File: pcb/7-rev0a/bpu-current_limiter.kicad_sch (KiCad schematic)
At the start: 44 parts, among them Q401 BCM857, Q402 BC2301T 2.8A, Q601 MMDT3906, Q602 BC2301T 2.8A, U4 MCP4725xxx-xCH, U5 MCP4725xxx-xCH, U601 GS321A-TR, U602 GSV331-TR

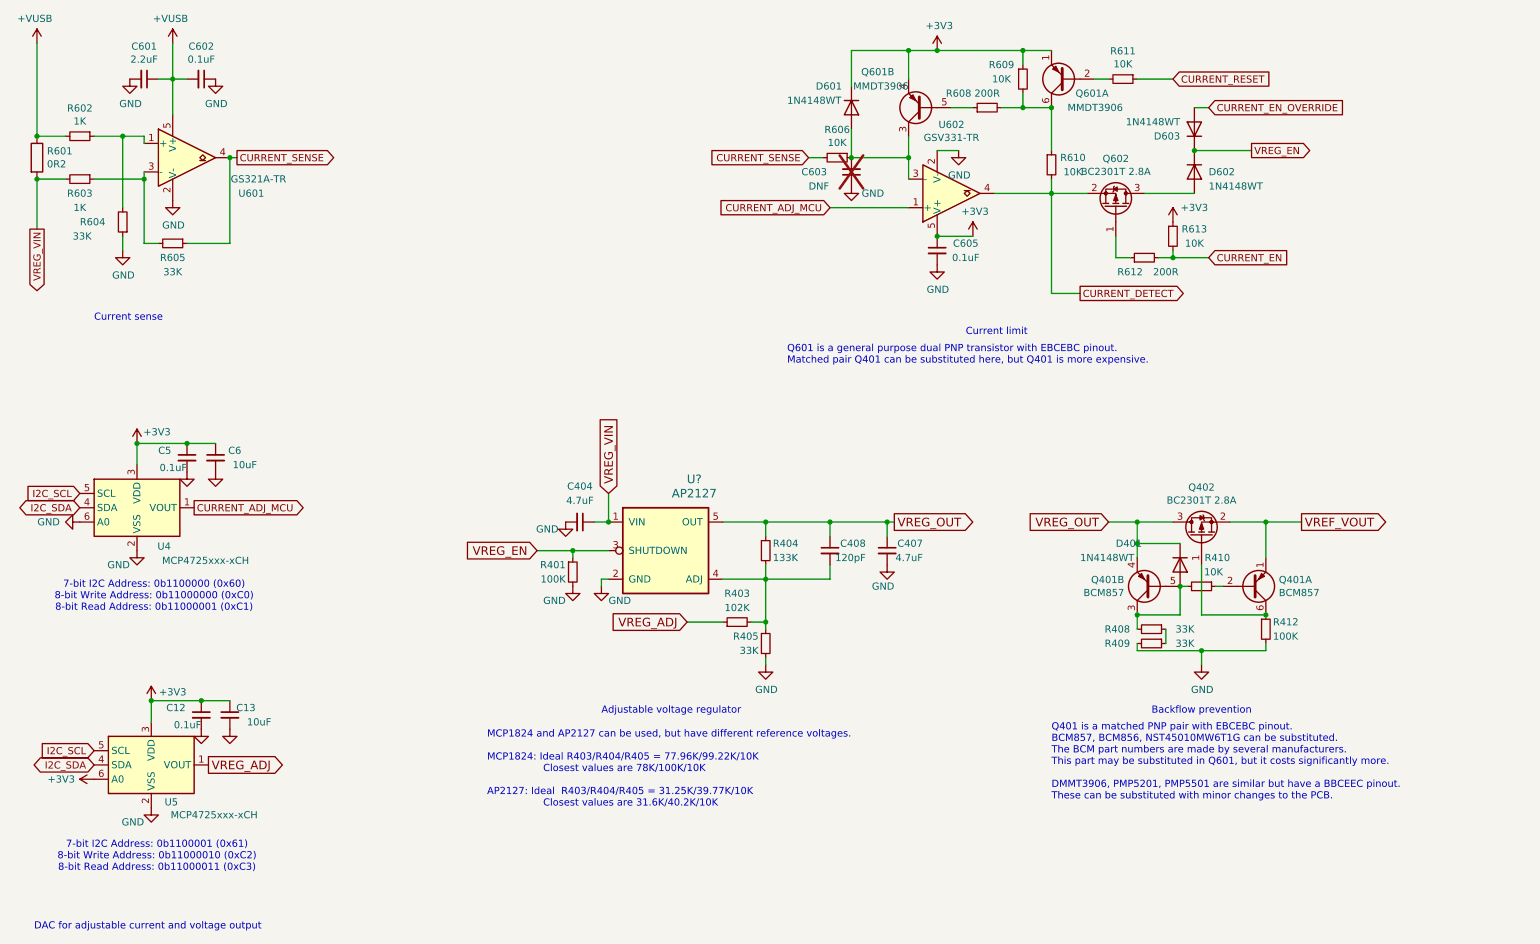
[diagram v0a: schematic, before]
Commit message: BP7 REV 0a: 2.2uF, 4.7uF -> 10uF/6.3V CL05A106MQ5NUN
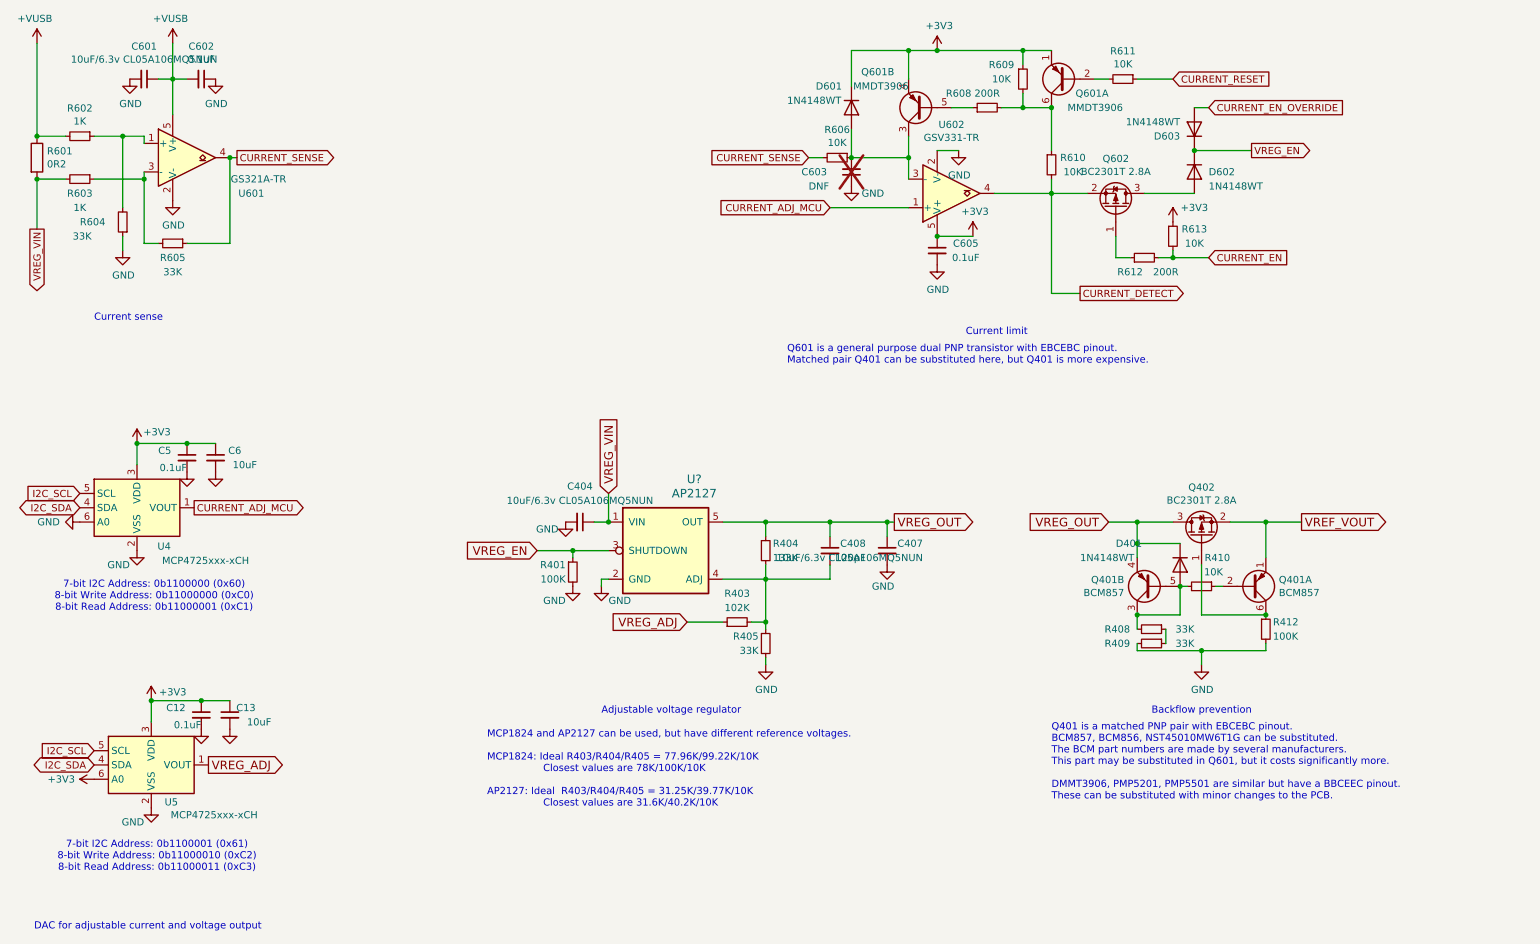
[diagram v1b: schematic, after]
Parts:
- C404, C407: value 4.7uF -> 10uF/6.3v CL05A106MQ5NUN
- C601: value 2.2uF -> 10uF/6.3v CL05A106MQ5NUN
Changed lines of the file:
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@@
 			)
 		)
-		(property "Value" "4.7uF"
+		(property "Value" "10uF/6.3v CL05A106MQ5NUN"
 			(at 179.07 113.03 0)
 			(effects
@@
 			)
 		)
-		(property "Value" "4.7uF"
+		(property "Value" "10uF/6.3v CL05A106MQ5NUN"
 			(at 118.11 102.87 90)
 			(effects
@@
 			)
 		)
-		(property "Value" "2.2uF"
+		(property "Value" "10uF/6.3v CL05A106MQ5NUN"
 			(at 40.64 24.4348 90)
 			(effects
